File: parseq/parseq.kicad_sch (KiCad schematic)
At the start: 46 parts, among them J1 Conn_01x01, J2 Conn_01x01, J3 Conn_01x01, J4 Conn_01x01, U1 Opamp_Quad, U2 Opamp_Dual

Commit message: update board
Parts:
- removed R14: 100, 1_trevortjes_lib:R_1x4, symbol 1_effects:Resistor
- added C13: 100u, 1_trevortjes_lib:CP_ELCO_1x2_S, symbol 1_effects:Capacitor_Polarized
- added R22, R23: 100, 1_trevortjes_lib:R_1x4, symbol 1_effects:Resistor
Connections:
- net GND: now also C13.2
- net at C3.1, U1.4 (V+): now also R23.2; no longer R15.1, U2.8 (V+)
- net at R13.2, R5.1, R6.1: now also U1.2 (-); no longer U1.9 (-)
- net at D1.1 (K): now also R15.1, R22.1, R23.1
- net at R11.1, R4.1, RV3.3: now also U1.3 (+); no longer U1.10 (+)
- net at C5.1, R4.2, RV1.6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: now also U1.10 (+); no longer U1.3 (+)
- net at C7.1, R19.2, R9.2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: now also U1.8; no longer U1.1
- net at C7.2, R10.2, R9.1: now also U1.9 (-); no longer U1.2 (-)
- net at R6.2, RV1.3 (6): now also U1.1; no longer U1.8
- new net: C13.1, R22.2, U2.8 (V+)
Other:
- moved on the sheet: C4, D1, R15, R16, U1A, U1C

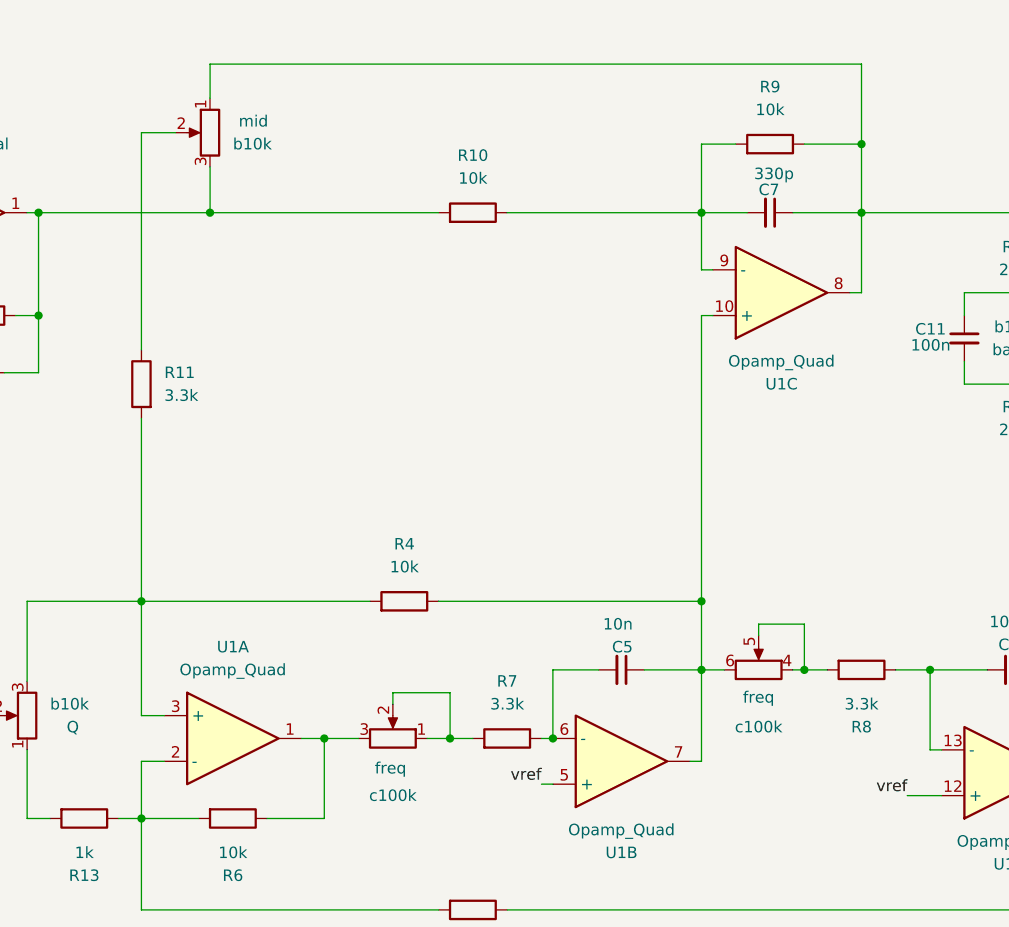
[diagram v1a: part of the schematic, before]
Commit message: add name and version to silkscreen
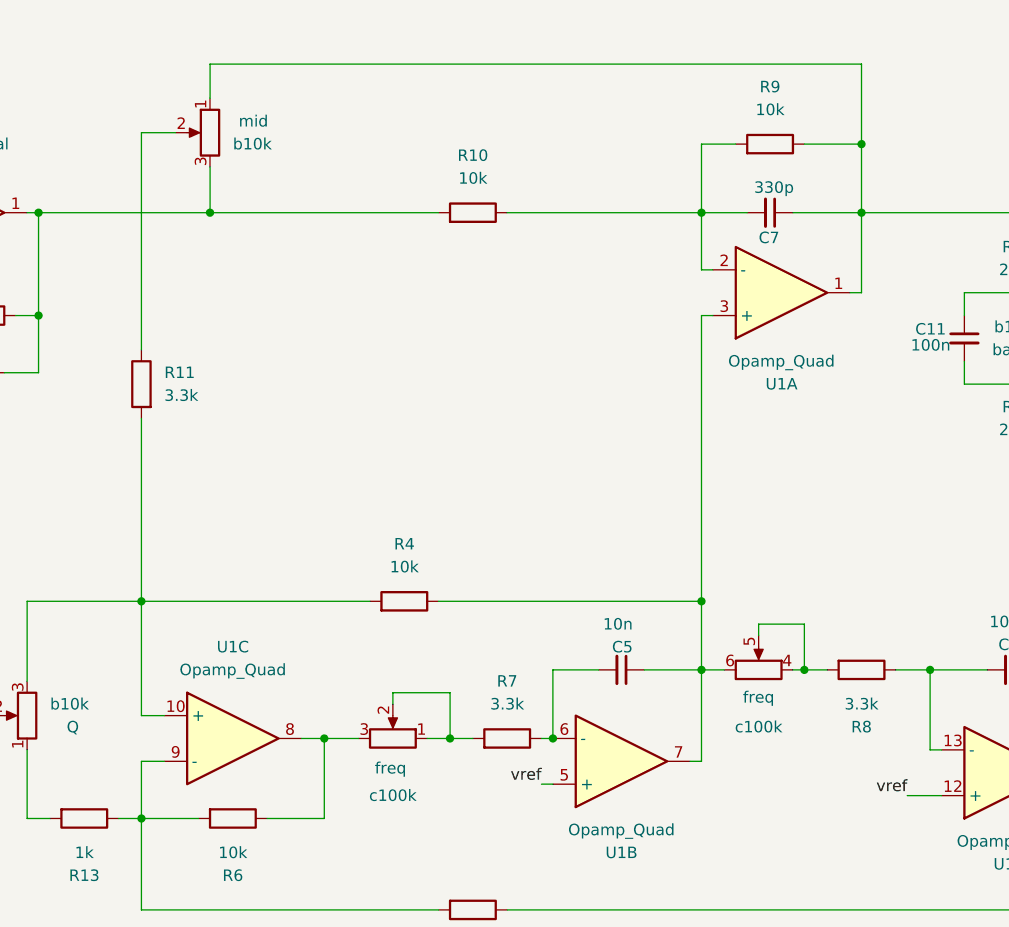
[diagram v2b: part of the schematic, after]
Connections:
- net at R13.2, R5.1, R6.1: now also U1.9 (-); no longer U1.2 (-)
- net at R11.1, R4.1, RV3.3: now also U1.10 (+); no longer U1.3 (+)
- net at C5.1, R4.2, RV1.6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: now also U1.3 (+); no longer U1.10 (+)
- net at C7.1, R19.2, R9.2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: now also U1.1; no longer U1.8
- net at C7.2, R10.2, R9.1: now also U1.2 (-); no longer U1.9 (-)
- net at R6.2, RV1.3 (6): now also U1.8; no longer U1.1
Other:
- moved on the sheet: U1A, U1C
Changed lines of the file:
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@@
 		(dnp no)
 		(property "Reference" "C7"
-			(at 149.8535 50.8 0)
+			(at 149.86 56.134 0)
 			(effects
 				(font
@@
 		)
 		(property "Value" "330p"
-			(at 149.352 49.022 0)
+			(at 149.352 50.546 0)
 			(effects
 				(font
@@
 	(symbol
 		(lib_id "Device:Opamp_Quad")
-		(at 91.44 111.76 0)
+		(at 152.4 62.23 0)
+		(mirror x)
 		(unit 1)
 		(exclude_from_sim no)
@@
 		(dnp no)
 		(property "Reference" "U1"
-			(at 91.44 101.6 0)
+			(at 152.4 72.39 0)
 			(effects
 				(font
@@
 		)
 		(property "Value" "Opamp_Quad"
-			(at 91.44 104.14 0)
+			(at 152.4 69.85 0)
 			(effects
 				(font
@@
 		)
 		(property "Footprint" "1_trevortjes_lib:DIP-14"
-			(at 91.44 111.76 0)
+			(at 152.4 62.23 0)
 			(effects
 				(font
@@
 		)
 		(property "Datasheet" "~"
-			(at 91.44 111.76 0)
+			(at 152.4 62.23 0)
 			(effects
 				(font
@@
 		)
 		(property "Description" "Quad operational amplifier"
-			(at 91.44 111.76 0)
+			(at 152.4 62.23 0)
 			(effects
 				(font
@@
 		)
 		(property "Sim.Library" "${KICAD9_SYMBOL_DIR}/Simulation_SPICE.sp"
-			(at 91.44 111.76 0)
+			(at 152.4 62.23 0)
 			(effects
 				(font
@@
 		)
 		(property "Sim.Name" "kicad_builtin_opamp_quad"
-			(at 91.44 111.76 0)
+			(at 152.4 62.23 0)
 			(effects
 				(font
@@
 		)
 		(property "Sim.Device" "SUBCKT"
-			(at 91.44 111.76 0)
+			(at 152.4 62.23 0)
 			(effects
 				(font
@@
 		)
 		(property "Sim.Pins" "1=out1 2=in1- 3=in1+ 4=vcc 5=in2+ 6=in2- 7=out2 8=out3 9=in3- 10=in3+ 11=vee 12=in4+ 13=in4- 14=out4"
-			(at 91.44 111.76 0)
+			(at 152.4 62.23 0)
 			(effects
 				(font
@@
 	(symbol
 		(lib_id "Device:Opamp_Quad")
-		(at 152.4 62.23 0)
-		(mirror x)
+		(at 91.44 111.76 0)
 		(unit 3)
 		(exclude_from_sim no)
@@
 		(dnp no)
 		(property "Reference" "U1"
-			(at 152.4 72.39 0)
+			(at 91.44 101.6 0)
 			(effects
 				(font
@@
 		)
 		(property "Value" "Opamp_Quad"
-			(at 152.4 69.85 0)
+			(at 91.44 104.14 0)
 			(effects
 				(font
@@
 		)
 		(property "Footprint" "1_trevortjes_lib:DIP-14"
-			(at 152.4 62.23 0)
+			(at 91.44 111.76 0)
 			(effects
 				(font
@@
 		)
 		(property "Datasheet" "~"
-			(at 152.4 62.23 0)
+			(at 91.44 111.76 0)
 			(effects
 				(font
@@
 		)
 		(property "Description" "Quad operational amplifier"
-			(at 152.4 62.23 0)
+			(at 91.44 111.76 0)
 			(effects
 				(font
@@
 		)
 		(property "Sim.Library" "${KICAD9_SYMBOL_DIR}/Simulation_SPICE.sp"
-			(at 152.4 62.23 0)
+			(at 91.44 111.76 0)
 			(effects
 				(font
@@
 		)
 		(property "Sim.Name" "kicad_builtin_opamp_quad"
-			(at 152.4 62.23 0)
+			(at 91.44 111.76 0)
 			(effects
 				(font
@@
 		)
 		(property "Sim.Device" "SUBCKT"
-			(at 152.4 62.23 0)
+			(at 91.44 111.76 0)
 			(effects
 				(font
@@
 		)
 		(property "Sim.Pins" "1=out1 2=in1- 3=in1+ 4=vcc 5=in2+ 6=in2- 7=out2 8=out3 9=in3- 10=in3+ 11=vee 12=in4+ 13=in4- 14=out4"
-			(at 152.4 62.23 0)
+			(at 91.44 111.76 0)
 			(effects
 				(font
